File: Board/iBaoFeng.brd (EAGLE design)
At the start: 100 x 80 mm, 9 parts

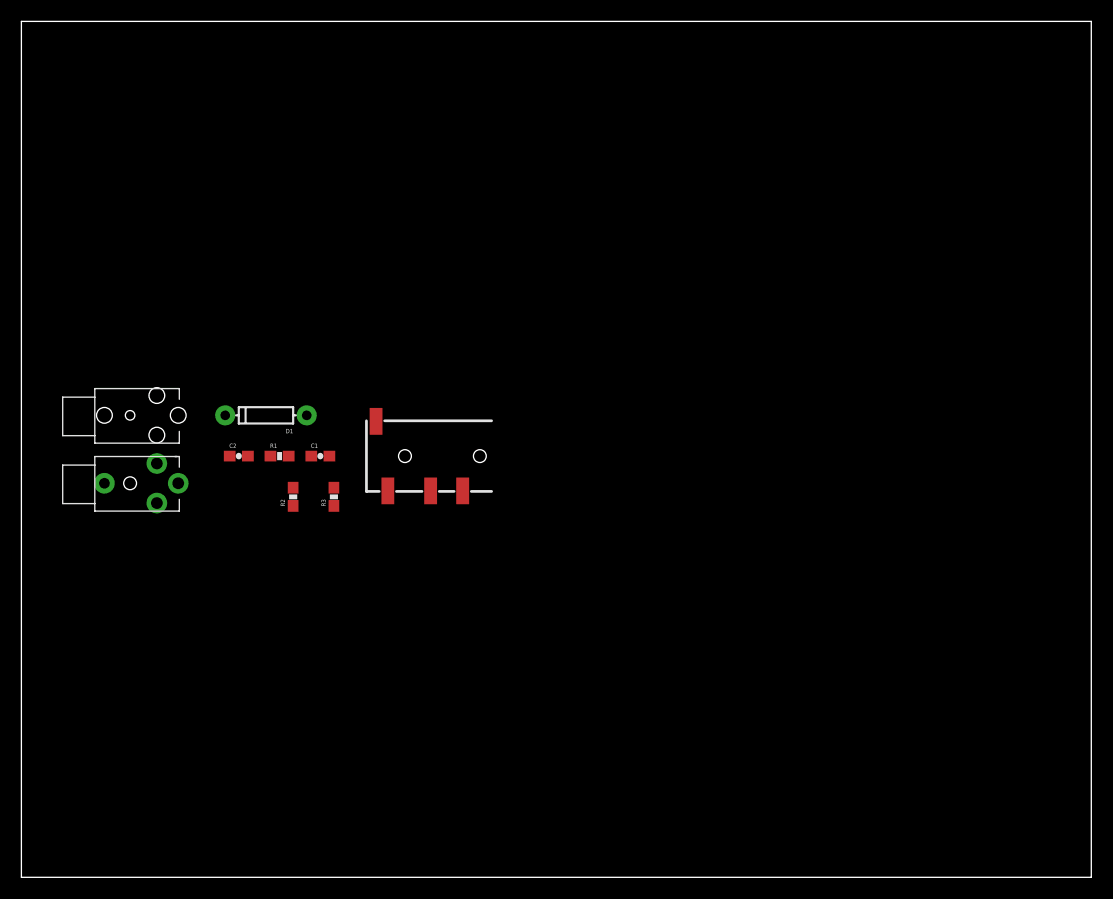
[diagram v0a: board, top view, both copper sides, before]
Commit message: Changed from audio jacks to headers
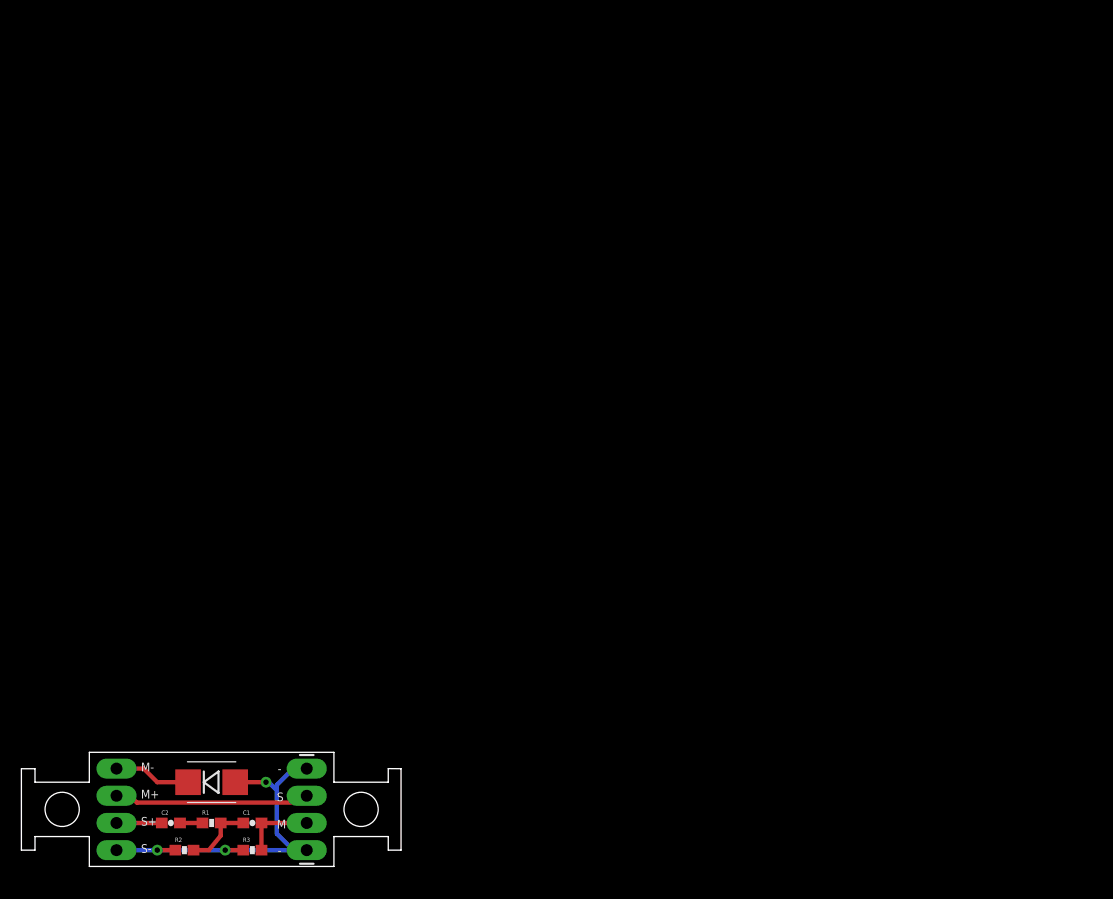
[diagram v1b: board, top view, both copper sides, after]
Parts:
- removed BAOFENG2.5SPK: (no value), SparkFun-Connectors:STEREOJACK2.5MM_STEREOJACK2.5MM
- removed BAOFENG3.5MIC: (no value), SparkFun-Connectors:STEREOJACK2.5MM_SPECIAL_HOLES-ONLY
- removed IPHONE: AUDIO-JACK3, SparkFun-Connectors:AUDIO-JACK-TRRS-SMD
- added JP1, JP2: M02PTH3, SparkFun-Connectors:1X02_LONGPADS
- added JP3: (no value), SparkFun-Connectors:1X04_LONGPADS
- D1: device SparkFun-DiscreteSemi:DIODE-1N4148 -> SparkFun-DiscreteSemi:SMB-DIODE
- moved C1 34.9 mm to (21.6, 5.08)
- moved C2 34.9 mm to (14.0, 5.08), turned to 180 degrees
- moved R1 34.9 mm to (17.8, 5.08)
- moved D1 34.7 mm to (17.8, 8.89), turned to 0 degrees
- moved R2 34.5 mm to (15.2, 2.54), turned to 0 degrees
- moved R3 33.9 mm to (21.6, 2.54), turned to 0 degrees
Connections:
- net BAOFENGMIC+: now also JP2.1, JP3.3; no longer BAOFENG3.5MIC.TIP, IPHONE.TIP
- net BAOFENGMIC-: now also JP2.2; no longer BAOFENG3.5MIC.RING1
- net BAOFENGSPK+: now also JP1.1; no longer BAOFENG2.5SPK.SHIELD
- net GND: now also JP1.2, JP3.1, JP3.4; no longer BAOFENG2.5SPK.RING1, IPHONE.RING2
- net N$4: now also JP3.2; no longer IPHONE.EARTH
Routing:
- net GND: track 0.00 -> 35.5 mm, vias 0 -> 3
- net BAOFENGMIC+: track 0.00 -> 18.3 mm
- net BAOFENGMIC-: track 0.00 -> 7.22 mm
- net N$4: track 0.00 -> 6.77 mm
- net N$3: track 0.00 -> 6.48 mm
- net BAOFENGSPK+: track 0.00 -> 4.23 mm
- net N$6: track 0.00 -> 2.11 mm
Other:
- board size 100 x 80 mm -> 35.5 x 10.7 mm
- board text added: "-"
- board text added: "Baofeng UV5R TRRS Adapter"
- board text added: "John Boiles KK6GIP"
- board text added: "M"
- board text added: "M+"
- board text added: "M-"
- board text added: "S"
- board text added: "S+"
- board text added: "S-"
- board text added: "r1"
